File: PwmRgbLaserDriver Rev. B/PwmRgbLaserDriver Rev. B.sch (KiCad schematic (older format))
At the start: 55 parts, among them IC1 ADA4817-1ARDZ, IC2 ADA4817-1ARDZ, IC3 ADA4817-1ARDZ, J1 RED_IN, J2 15V, J3 RLO, J4 GREEN_IN, J5 GLO, J6 BLUE_IN, J7 BLO, Q1 Q_NPN_BCE, Q2 Q_NPN_BCE, Q3 Q_NPN_BCE, U1 TPS54331GDR

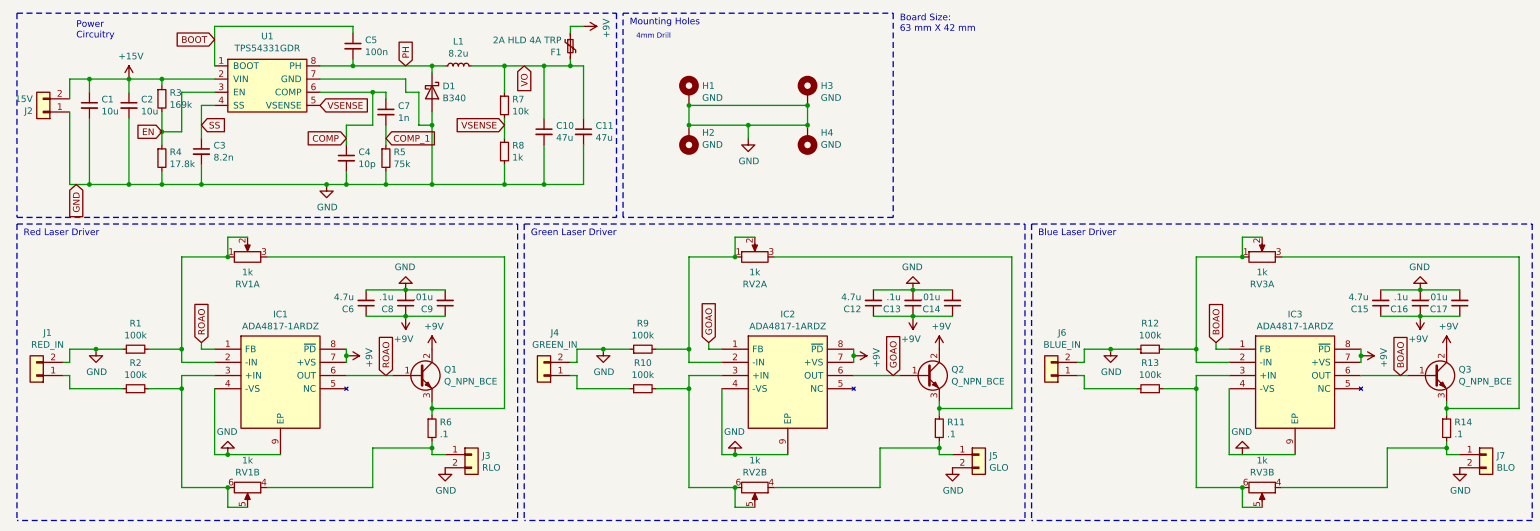
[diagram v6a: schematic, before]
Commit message: Placement And Some Routhing
Placed all components and routed the important analog signal traces.
Power remains unfinished along with precise placement of the mounting holes.
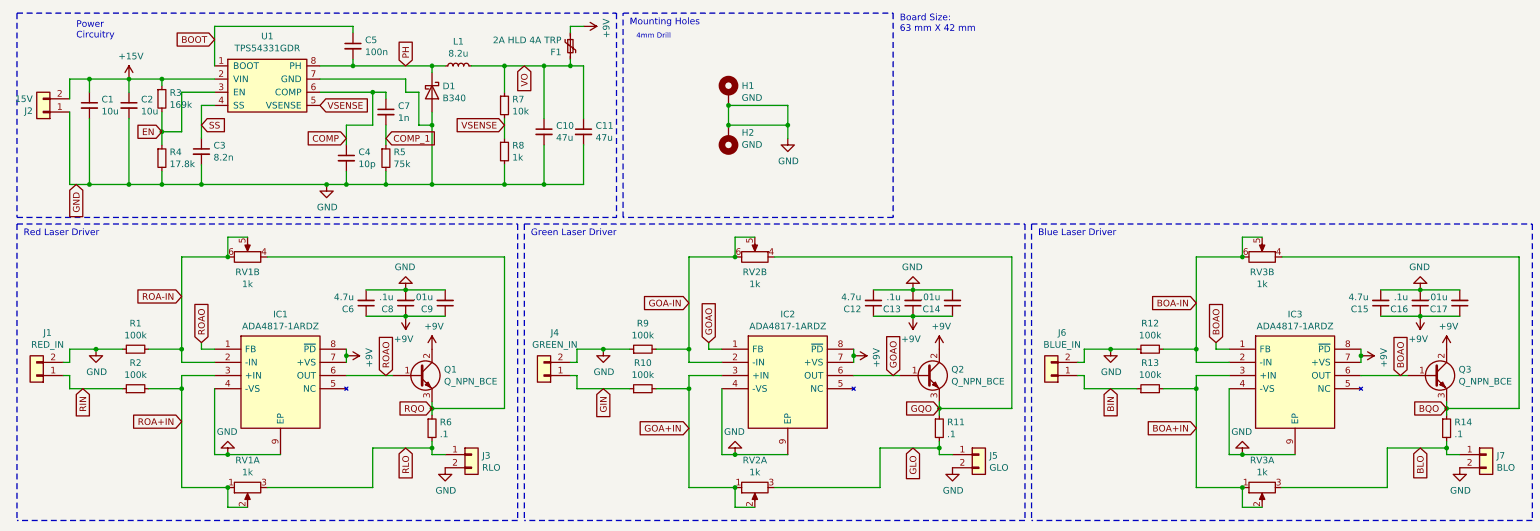
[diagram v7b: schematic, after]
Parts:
- removed H3, H4: GND, SamacSys_Parts:4mm Mounting Hole, symbol Mechanical:MountingHole_Pad
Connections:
- net GND: now also IC3.4 (-VS), IC3.9 (EP)
- net ROA+IN: now reaches RV1.1, RV1.2
- net ROA+IN: now also IC1.3 (+IN), R2.2; no longer IC1.2 (-IN), R1.2
- net ROA-IN: now reaches RV1.5, RV1.6
- net ROA-IN: now also IC1.2 (-IN), R1.2; no longer IC1.3 (+IN), R2.2
- net RQO: now reaches Q1.3 (E), R6.1
- net RQO: now also RV1.4; no longer RV1.3
- net RLO: now reaches J3.1 (Pin_1), R6.2
- net RLO: now also RV1.3; no longer RV1.4
- net RIN: now reaches J1.1 (Pin_1), R2.1
- net GOA+IN: now reaches RV2.1, RV2.2
- net GOA+IN: now also IC2.3 (+IN), R10.2; no longer IC2.2 (-IN), R9.2
- net GOA-IN: now reaches RV2.5, RV2.6
- net GOA-IN: now also IC2.2 (-IN), R9.2; no longer IC2.3 (+IN), R10.2
- net GQO: now reaches Q2.3 (E), R11.1
- net GQO: now also RV2.4; no longer RV2.3
- net GLO: now reaches J5.1 (Pin_1), R11.2
- net GLO: now also RV2.3; no longer RV2.4
- net GIN: now reaches J4.1 (Pin_1), R10.1
- net BOA+IN: now reaches RV3.1, RV3.2
- net BOA+IN: now also IC3.3 (+IN), R13.2; no longer IC3.2 (-IN), R12.2
- net BOA-IN: now reaches RV3.5, RV3.6
- net BOA-IN: now also IC3.2 (-IN), R12.2; no longer IC3.3 (+IN), R13.2
- net BQO: now reaches Q3.3 (E), R14.1
- net BQO: now also RV3.4; no longer RV3.3
- net BLO: now reaches J7.1 (Pin_1), R14.2
- net BLO: now also RV3.3; no longer RV3.4
- net BIN: now reaches J6.1 (Pin_1), R13.1
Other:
- moved on the sheet: H1, H2, RV1A, RV1B, RV2A, RV2B, RV3A, RV3B
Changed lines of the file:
@@
 L Device:R_POT_Dual_Separate RV1
 U 1 1 60DDA5AF
+P 2250 4100
+F 0 "RV1" V 2043 4100 50  0000 C CNN
+F 1 "1k" V 2134 4100 50  0000 C CNN
+F 2 "SamacSys_Parts:DualGangPotAmazon" H 2250 4100 50  0001 C CNN
+F 3 "~" H 2250 4100 50  0001 C CNN
+	1    2250 4100
+	0    -1   1    0
+$EndComp
+$Comp
+L Device:R_POT_Dual_Separate RV1
+U 2 1 60DDB4D9
 P 2250 2350
-F 0 "RV1" V 2043 2350 50  0000 C CNN
-F 1 "1k" V 2134 2350 50  0000 C CNN
+F 0 "RV1" V 2135 2350 50  0000 C CNN
+F 1 "1k" V 2044 2350 50  0000 C CNN
 F 2 "SamacSys_Parts:DualGangPotAmazon" H 2250 2350 50  0001 C CNN
 F 3 "~" H 2250 2350 50  0001 C CNN
-	1    2250 2350
-	0    -1   -1   0
-$EndComp
-$Comp
-L Device:R_POT_Dual_Separate RV1
-U 2 1 60DDB4D9
-P 2250 4100
-F 0 "RV1" V 2135 4100 50  0000 C CNN
-F 1 "1k" V 2044 4100 50  0000 C CNN
-F 2 "SamacSys_Parts:DualGangPotAmazon" H 2250 4100 50  0001 C CNN
-F 3 "~" H 2250 4100 50  0001 C CNN
-	2    2250 4100
-	0    1    1    0
+	2    2250 2350
+	0    1    -1   0
 $EndComp
 $Comp
@@
 Wire Wire Line
 	2100 2350 1750 2350
-Connection ~ 2100 2350
 Connection ~ 1750 3050
 Wire Wire Line
@@
 	1750 4100 2100 4100
 Connection ~ 1750 3350
-Connection ~ 2100 4100
 Wire Wire Line
 	2400 4100 3200 4100
@@
 L Device:R_POT_Dual_Separate RV2
 U 1 1 60E617B4
+P 6100 4100
+F 0 "RV2" V 5893 4100 50  0000 C CNN
+F 1 "1k" V 5984 4100 50  0000 C CNN
+F 2 "SamacSys_Parts:DualGangPotAmazon" H 6100 4100 50  0001 C CNN
+F 3 "~" H 6100 4100 50  0001 C CNN
+	1    6100 4100
+	0    -1   1    0
+$EndComp
+$Comp
+L Device:R_POT_Dual_Separate RV2
+U 2 1 60E617BA
 P 6100 2350
-F 0 "RV2" V 5893 2350 50  0000 C CNN
-F 1 "1k" V 5984 2350 50  0000 C CNN
+F 0 "RV2" V 5985 2350 50  0000 C CNN
+F 1 "1k" V 5894 2350 50  0000 C CNN
 F 2 "SamacSys_Parts:DualGangPotAmazon" H 6100 2350 50  0001 C CNN
 F 3 "~" H 6100 2350 50  0001 C CNN
-	1    6100 2350
-	0    -1   -1   0
-$EndComp
-$Comp
-L Device:R_POT_Dual_Separate RV2
-U 2 1 60E617BA
-P 6100 4100
-F 0 "RV2" V 5985 4100 50  0000 C CNN
-F 1 "1k" V 5894 4100 50  0000 C CNN
-F 2 "SamacSys_Parts:DualGangPotAmazon" H 6100 4100 50  0001 C CNN
-F 3 "~" H 6100 4100 50  0001 C CNN
-	2    6100 4100
-	0    1    1    0
+	2    6100 2350
+	0    1    -1   0
 $EndComp
 $Comp
@@
 Wire Wire Line
 	5950 2350 5600 2350
-Connection ~ 5950 2350
 Connection ~ 5600 3050
 Wire Wire Line
@@
 	5600 4100 5950 4100
 Connection ~ 5600 3350
-Connection ~ 5950 4100
 Wire Wire Line
 	6250 4100 7050 4100
@@
 L Device:R_POT_Dual_Separate RV3
 U 1 1 60E84C72
+P 9950 4100
+F 0 "RV3" V 9743 4100 50  0000 C CNN
+F 1 "1k" V 9834 4100 50  0000 C CNN
+F 2 "SamacSys_Parts:DualGangPotAmazon" H 9950 4100 50  0001 C CNN
+F 3 "~" H 9950 4100 50  0001 C CNN
+	1    9950 4100
+	0    -1   1    0
+$EndComp
+$Comp
+L Device:R_POT_Dual_Separate RV3
+U 2 1 60E84C78
 P 9950 2350
-F 0 "RV3" V 9743 2350 50  0000 C CNN
-F 1 "1k" V 9834 2350 50  0000 C CNN
+F 0 "RV3" V 9835 2350 50  0000 C CNN
+F 1 "1k" V 9744 2350 50  0000 C CNN
 F 2 "SamacSys_Parts:DualGangPotAmazon" H 9950 2350 50  0001 C CNN
 F 3 "~" H 9950 2350 50  0001 C CNN
-	1    9950 2350
-	0    -1   -1   0
-$EndComp
-$Comp
-L Device:R_POT_Dual_Separate RV3
-U 2 1 60E84C78
-P 9950 4100
-F 0 "RV3" V 9835 4100 50  0000 C CNN
-F 1 "1k" V 9744 4100 50  0000 C CNN
-F 2 "SamacSys_Parts:DualGangPotAmazon" H 9950 4100 50  0001 C CNN
-F 3 "~" H 9950 4100 50  0001 C CNN
-	2    9950 4100
-	0    1    1    0
+	2    9950 2350
+	0    1    -1   0
 $EndComp
 $Comp
@@
 	9700 3350 9700 3850
 Wire Wire Line
-	9700 3850 10200 3850
-Wire Wire Line
 	9800 2350 9800 2200
 $Comp
@@
 Wire Wire Line
 	9800 2350 9450 2350
-Connection ~ 9800 2350
 Connection ~ 9450 3050
 Wire Wire Line
@@
 	9450 4100 9800 4100
 Connection ~ 9450 3350
-Connection ~ 9800 4100
 Wire Wire Line
 	10100 4100 10900 4100
@@
 L Mechanical:MountingHole_Pad H1
 U 1 1 60F218DC
-P 5600 1100
-F 0 "H1" H 5700 1149 50  0000 L CNN
-F 1 "GND" H 5700 1058 50  0000 L CNN
-F 2 "SamacSys_Parts:4mm Mounting Hole" H 5600 1100 50  0001 C CNN
-F 3 "~" H 5600 1100 50  0001 C CNN
-	1    5600 1100
-	1    0    0    -1
-$EndComp
-$Comp
-L Mechanical:MountingHole_Pad H3
-U 1 1 60F221AD
-P 6500 1100
-F 0 "H3" H 6600 1149 50  0000 L CNN
-F 1 "GND" H 6600 1058 50  0000 L CNN
-F 2 "SamacSys_Parts:4mm Mounting Hole" H 6500 1100 50  0001 C CNN
-F 3 "~" H 6500 1100 50  0001 C CNN
-	1    6500 1100
-	1    0    0    -1
-$EndComp
-$Comp
-L Mechanical:MountingHole_Pad H4
-U 1 1 60F2CC53
-P 6500 1450
-F 0 "H4" H 6400 1407 50  0000 R CNN
-F 1 "GND" H 6400 1498 50  0000 R CNN
-F 2 "SamacSys_Parts:4mm Mounting Hole" H 6500 1450 50  0001 C CNN
-F 3 "~" H 6500 1450 50  0001 C CNN
-	1    6500 1450
-	-1   0    0    1
+P 5900 1100
+F 0 "H1" H 6000 1149 50  0000 L CNN
+F 1 "GND" H 6000 1058 50  0000 L CNN
+F 2 "SamacSys_Parts:4mm Mounting Hole" H 5900 1100 50  0001 C CNN
+F 3 "~" H 5900 1100 50  0001 C CNN
+	1    5900 1100
+	1    0    0    -1
 $EndComp
 $Comp
 L Mechanical:MountingHole_Pad H2
 U 1 1 60F37841
-P 5600 1450
-F 0 "H2" H 5500 1407 50  0000 R CNN
-F 1 "GND" H 5500 1498 50  0000 R CNN
-F 2 "SamacSys_Parts:4mm Mounting Hole" H 5600 1450 50  0001 C CNN
-F 3 "~" H 5600 1450 50  0001 C CNN
-	1    5600 1450
-	-1   0    0    1
-$EndComp
-Wire Wire Line
-	5600 1200 5600 1350
-Wire Wire Line
-	6500 1350 6050 1350
-Connection ~ 5600 1350
-Wire Wire Line
-	5600 1200 6500 1200
-Connection ~ 5600 1200
-Wire Wire Line
-	6500 1200 6500 1350
-Connection ~ 6500 1200
-Connection ~ 6500 1350
+P 5900 1450
+F 0 "H2" H 5800 1407 50  0000 R CNN
+F 1 "GND" H 5800 1498 50  0000 R CNN
+F 2 "SamacSys_Parts:4mm Mounting Hole" H 5900 1450 50  0001 C CNN
+F 3 "~" H 5900 1450 50  0001 C CNN
+	1    5900 1450
+	-1   0    0    1
+$EndComp
+Wire Wire Line
+	5900 1200 5900 1350
+Connection ~ 5900 1350
 $Comp
 L power:GND #PWR0122
 U 1 1 60F81A6B
-P 6050 1450
-F 0 "#PWR0122" H 6050 1200 50  0001 C CNN
-F 1 "GND" H 6055 1277 50  0000 C CNN
-F 2 "" H 6050 1450 50  0001 C CNN
-F 3 "" H 6050 1450 50  0001 C CNN
-	1    6050 1450
-	1    0    0    -1
-$EndComp
-Wire Wire Line
-	6050 1450 6050 1350
-Connection ~ 6050 1350
-Wire Wire Line
-	6050 1350 5600 1350
+P 6350 1450
+F 0 "#PWR0122" H 6350 1200 50  0001 C CNN
+F 1 "GND" H 6355 1277 50  0000 C CNN
+F 2 "" H 6350 1450 50  0001 C CNN
+F 3 "" H 6350 1450 50  0001 C CNN
+	1    6350 1450
+	1    0    0    -1
+$EndComp
+Wire Wire Line
+	6350 1450 6350 1350
+Wire Wire Line
+	6350 1350 5900 1350
 Wire Notes Line
 	5100 500  7150 500
@@
 COMP_1
 $Comp
-L power:GND #PWR?
+L power:GND #PWR0123
 U 1 1 60F58E09
 P 9800 3850
-F 0 "#PWR?" H 9800 3600 50  0001 C CNN
+F 0 "#PWR0123" H 9800 3600 50  0001 C CNN
 F 1 "GND" H 9805 3677 50  0000 C CNN
 F 2 "" H 9800 3850 50  0001 C CNN
@@
 $EndComp
 $Comp
-L power:GND #PWR?
+L power:GND #PWR0124
 U 1 1 60F64D0D
 P 5950 3850
-F 0 "#PWR?" H 5950 3600 50  0001 C CNN
+F 0 "#PWR0124" H 5950 3600 50  0001 C CNN
 F 1 "GND" H 5955 3677 50  0000 C CNN
 F 2 "" H 5950 3850 50  0001 C CNN
@@
 	5950 3850 6350 3850
 $Comp
-L power:GND #PWR?
+L power:GND #PWR0125
 U 1 1 60F66A16
 P 2100 3850
-F 0 "#PWR?" H 2100 3600 50  0001 C CNN
+F 0 "#PWR0125" H 2100 3600 50  0001 C CNN
 F 1 "GND" H 2105 3677 50  0000 C CNN
 F 2 "" H 2100 3850 50  0001 C CNN
@@
 Wire Wire Line
 	2100 3850 2500 3850
+Wire Wire Line
+	6350 1350 6350 1200
+Wire Wire Line
+	6350 1200 5900 1200
+Connection ~ 6350 1350
+Connection ~ 5900 1200
+Text GLabel 1000 3350 3    50   Input ~ 0
+RIN
+Text GLabel 1750 3600 0    50   Input ~ 0
+ROA+IN
+Text GLabel 1750 2650 0    50   Input ~ 0
+ROA-IN
+Text GLabel 3450 3800 3    50   Input ~ 0
+RLO
+Text GLabel 7300 3800 3    50   Input ~ 0
+GLO
+Text GLabel 5600 3650 0    50   Input ~ 0
+GOA+IN
+Text GLabel 5600 2700 0    50   Input ~ 0
+GOA-IN
+Text GLabel 4950 3350 3    50   Input ~ 0
+GIN
+Text GLabel 9450 3650 0    50   Input ~ 0
+BOA+IN
+Text GLabel 8800 3350 3    50   Input ~ 0
+BIN
+Text GLabel 9450 2700 0    50   Input ~ 0
+BOA-IN
+Text GLabel 11150 3800 3    50   Input ~ 0
+BLO
+Wire Wire Line
+	9700 3850 9800 3850
+Wire Wire Line
+	9800 3850 10200 3850
+Connection ~ 9800 3850
+Connection ~ 2100 2350
+Connection ~ 2100 4100
+Connection ~ 5950 2350
+Connection ~ 5950 4100
+Connection ~ 9800 2350
+Connection ~ 9800 4100
+Text GLabel 3650 3500 0    50   Input ~ 0
+RQO
+Text GLabel 7500 3500 0    50   Input ~ 0
+GQO
+Text GLabel 11350 3500 0    50   Input ~ 0
+BQO
 $EndSCHEMATC
